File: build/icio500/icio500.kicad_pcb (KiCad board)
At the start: 4 copper layers, 147.6 x 105 mm, 56 parts, among them J1 ?, U1 ?, U2 ?, U3 ?, U4 ?, U5 ?, U6 ?

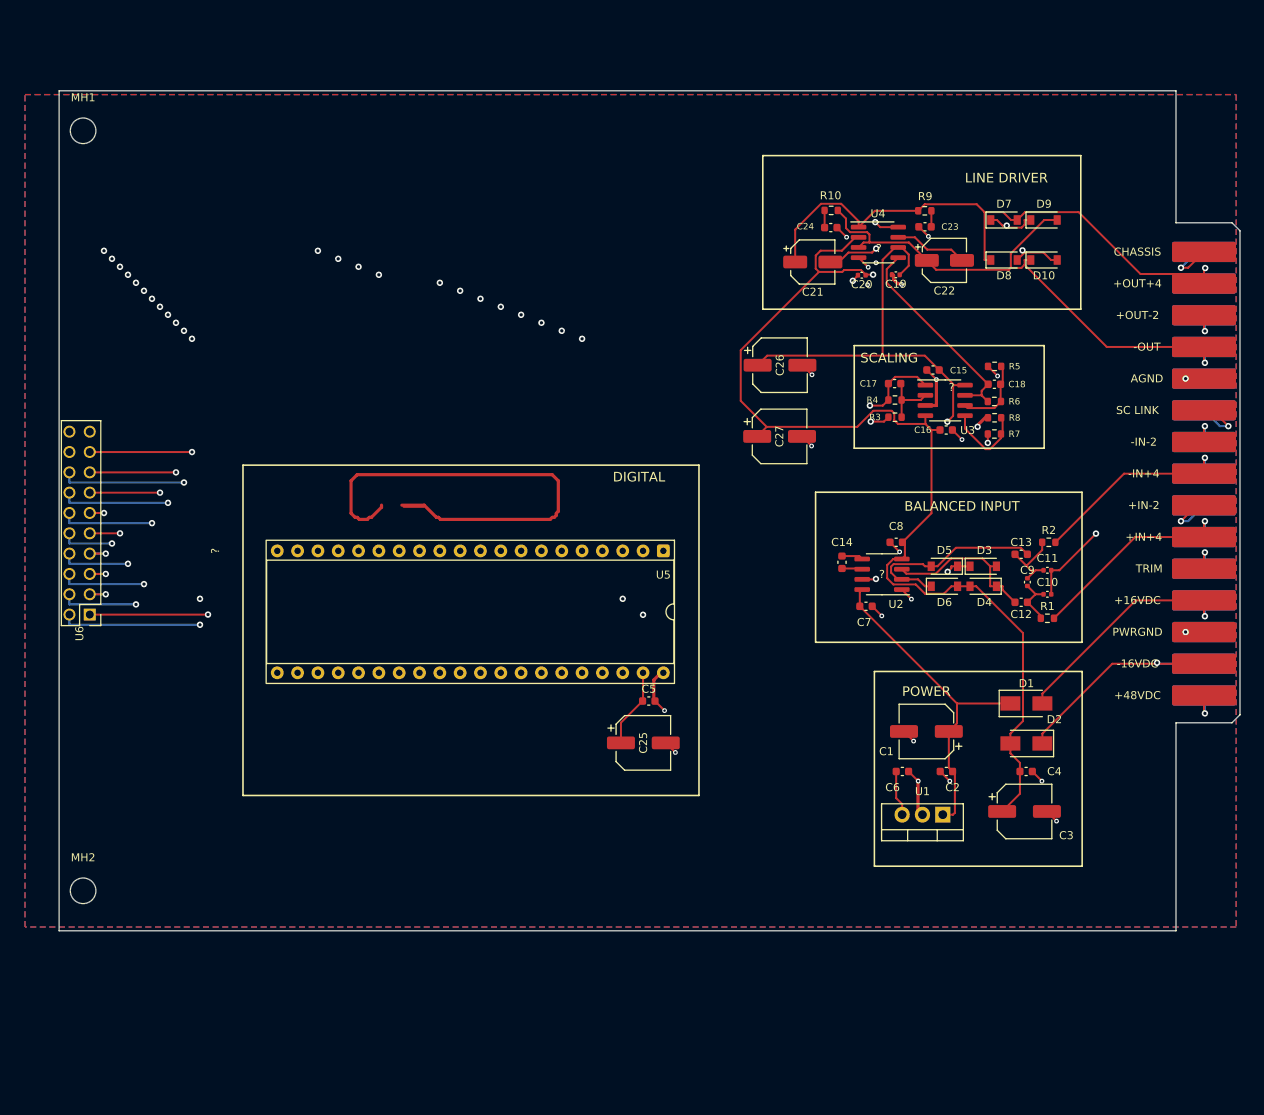
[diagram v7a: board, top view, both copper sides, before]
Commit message: Fix VPR-500 carrier edge cuts, center card tongue with zero bottom bulk, and align U6 header mating to 0.000mm
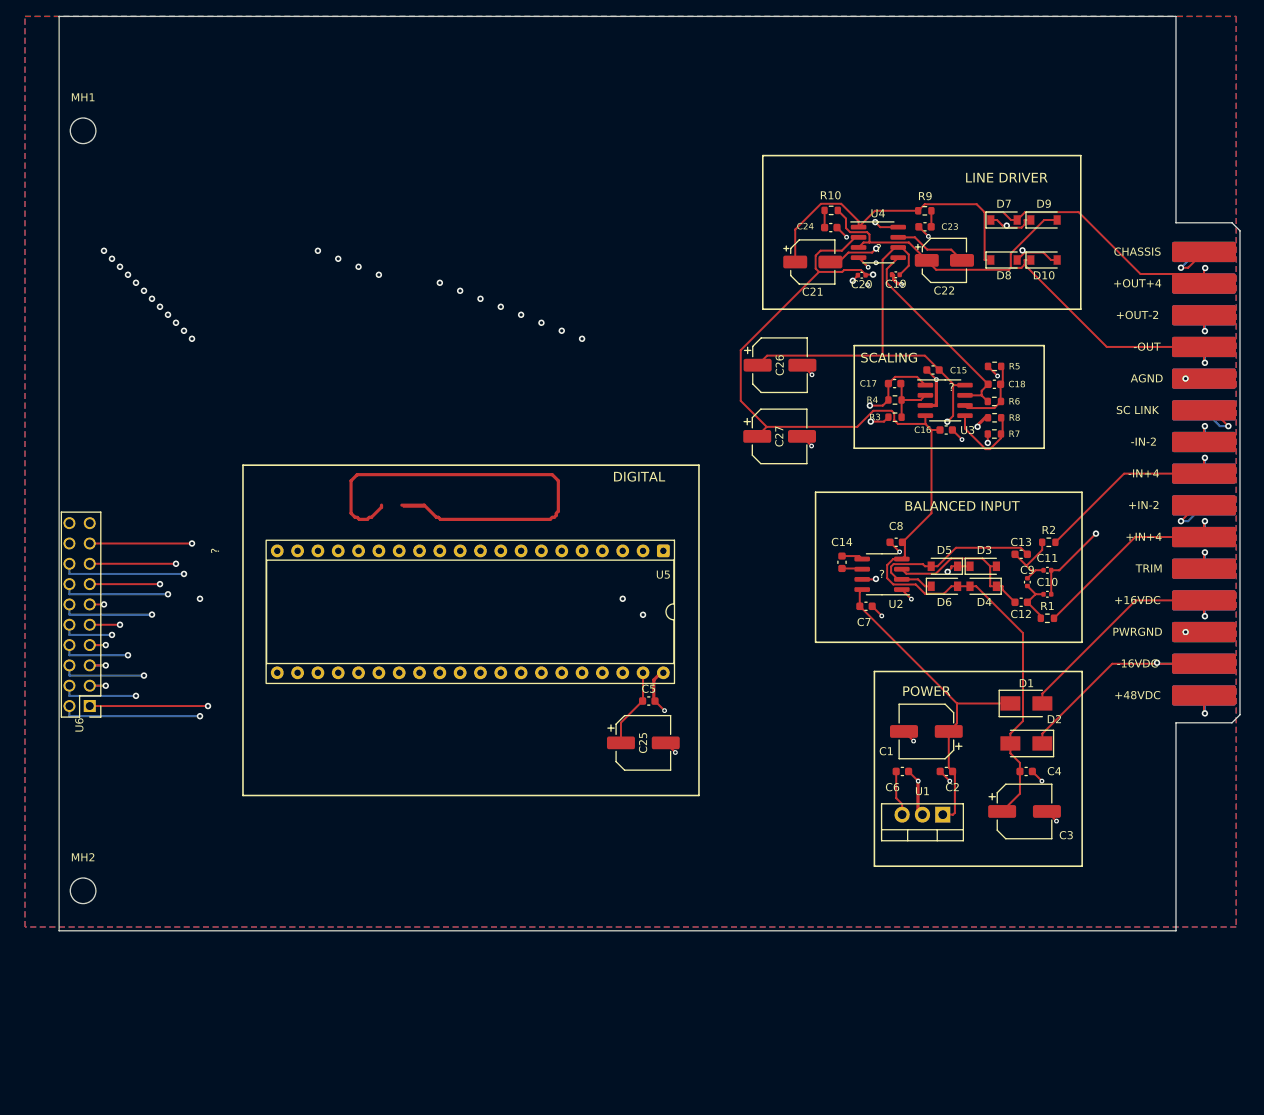
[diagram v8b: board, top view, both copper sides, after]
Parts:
- moved U6 11.4 mm to (59.2, 131.9)
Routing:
- net spi1_sck: track 110.7 -> 122.2 mm
- net spi1_miso: track 105.1 -> 116.6 mm
- net spi1_cs: track 103.7 -> 115.1 mm
- net gpio_enc_b: track 107.0 -> 118.4 mm
- net d14: track 102.4 -> 113.9 mm
- net d13: track 110.6 -> 122.0 mm
- net audio_in_r: track 82.9 -> 94.4 mm
- net gpio_enc_sw: track 98.8 -> 110.2 mm
- net gpio_disp_res: track 102.2 -> 113.6 mm
- net spi1_mosi: track 112.2 -> 123.6 mm
- net i2c1_sda: track 121.3 -> 132.7 mm
- net i2c1_scl: track 119.3 -> 130.7 mm
- net gpio_disp_dc: track 109.3 -> 120.7 mm
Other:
- board size 147.6 x 105 mm -> 147.6 x 114.3 mm
